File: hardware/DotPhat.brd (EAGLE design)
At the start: 30 x 65 mm, 39 parts, among them CN1 1X4-BIG, IC1 CAT24M010TS, J2 RASPBERRYPI-40-PIN-GPIO_PTH, J3 USB-MICROB, U1 ATMEGA328P-MU-QFN32, U2 TMP102, U3 ATSHA204-TSU, X3 S4B-ZR

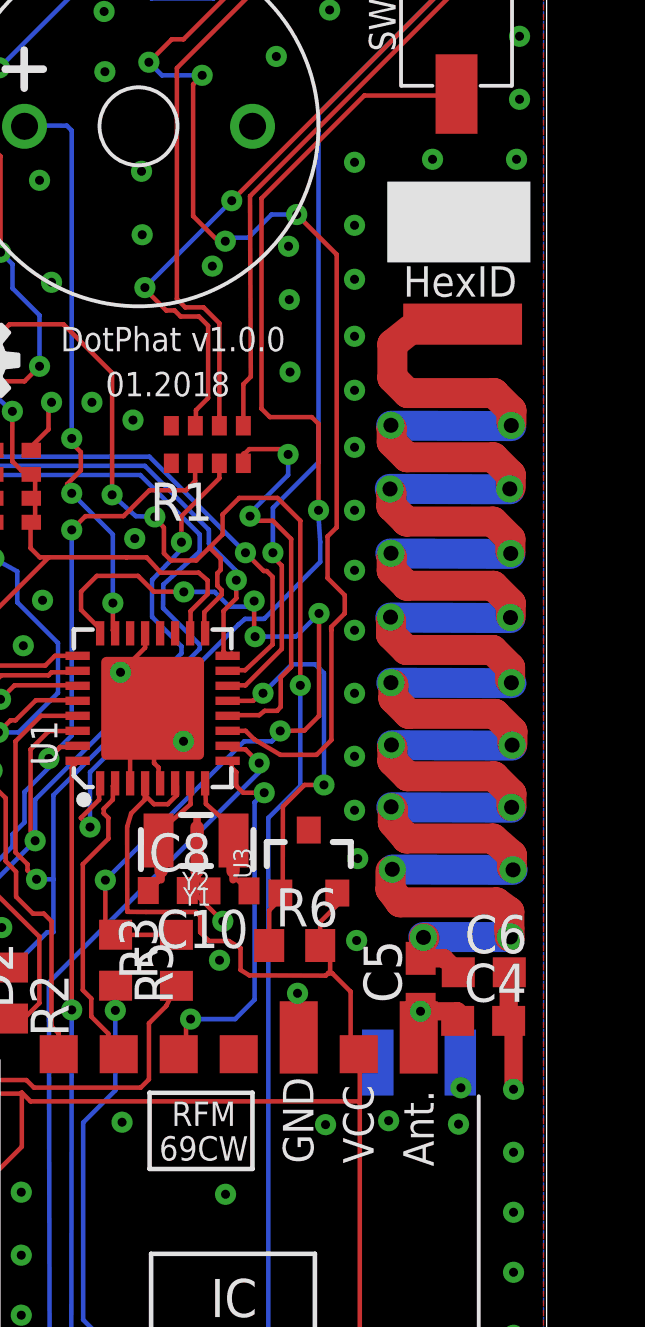
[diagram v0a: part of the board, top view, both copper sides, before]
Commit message: Flip uFL to top side
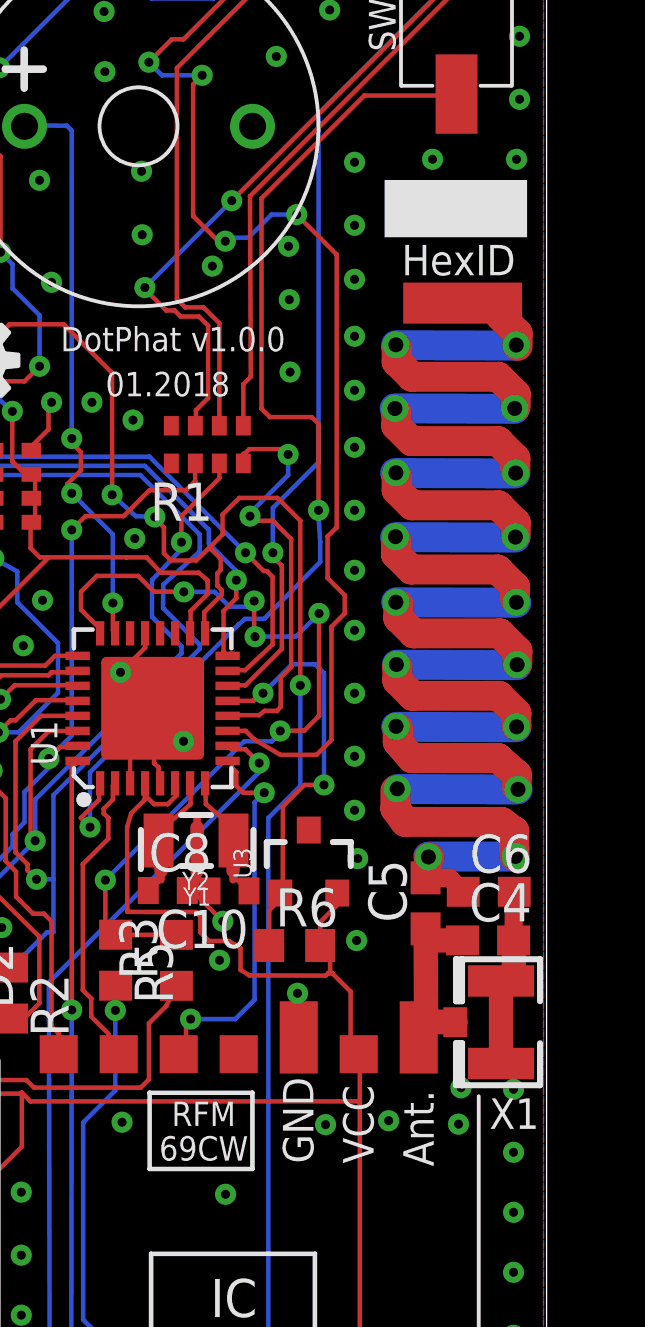
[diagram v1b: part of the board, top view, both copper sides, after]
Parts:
- moved X1 3.05 mm to (28.5, 21.5), flipped to the top, turned to 180 degrees
- moved C4 2.69 mm to (28.1, 24.3)
- moved C5 2.69 mm to (26.0, 25.5)
- moved C6 2.69 mm to (28.1, 25.9)
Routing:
- net ANT: track 86.7 -> 80.0 mm
- net ANT_OUT: track 3.57 -> 7.32 mm, vias 1 -> 0
- net GND: track 52.1 -> 54.0 mm
- net ANT2: track 0.00 -> 1.24 mm

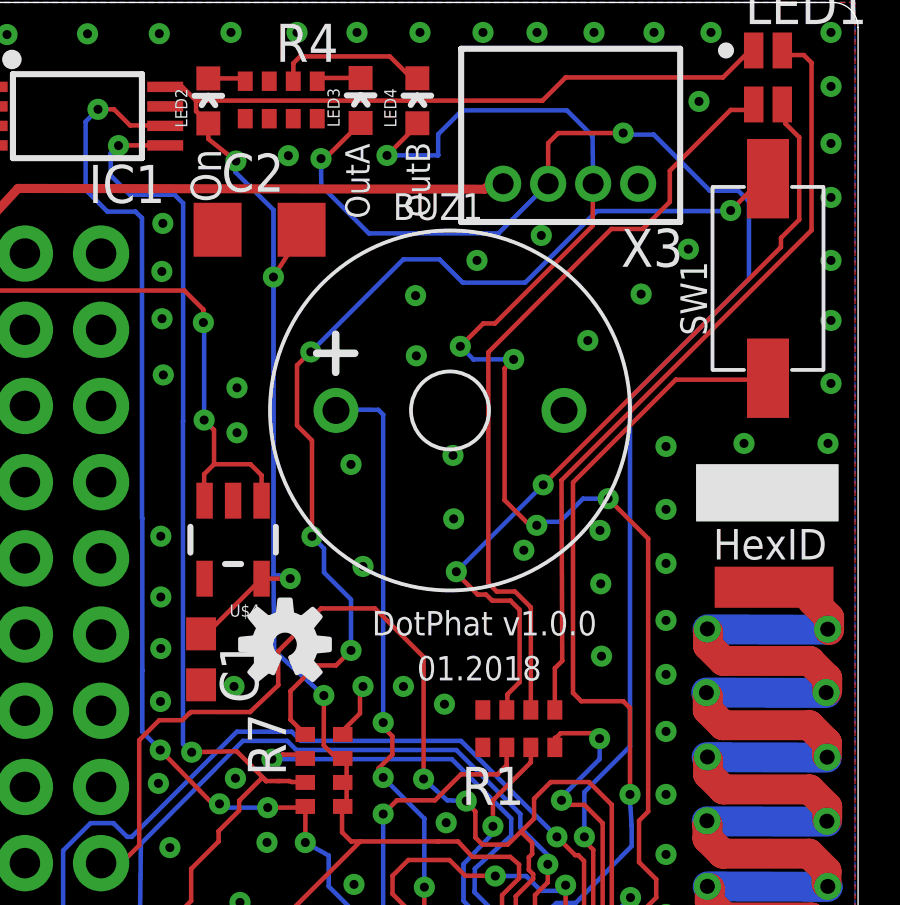
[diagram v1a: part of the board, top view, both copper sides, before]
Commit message: Switch to SMD buzzer
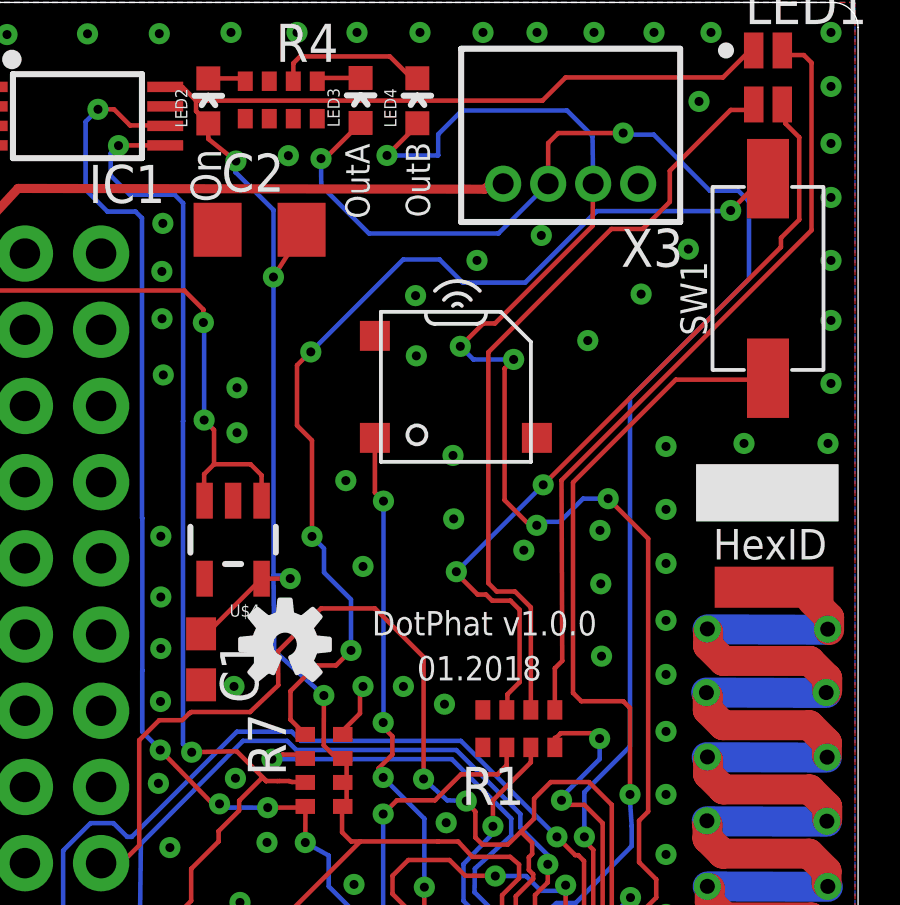
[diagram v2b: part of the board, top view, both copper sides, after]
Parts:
- removed BUZ1: KS-12065D03YA, Seeed-OPL-Connector:BZ2-7.6-D12.0XH6.5MM
- added SPK1: SMT-0540-S-R, adafruit:SMT-0540-S-R
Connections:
- net BUZZER: now also SPK1.+; no longer BUZ1.+
- net GND: now also SPK1.-; no longer BUZ1.-
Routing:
- net BUZZER: track 19.4 -> 17.1 mm, vias 3 -> 4
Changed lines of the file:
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@@
 <attribute name="PROD_ID" value="CONN-12263" x="3.5" y="32.5" size="1.778" layer="27" rot="R180" display="off"/>
-</element>
-<element name="BUZ1" library="Seeed-OPL-Connector" package="BZ2-7.6-D12.0XH6.5MM" value="KS-12065D03YA" x="16.4" y="51.4">
-<attribute name="MPN" value="KS-12065D03YA" x="16.4" y="51.4" size="1.778" layer="27" display="off"/>
 </element>
 <element name="LOGO1" library="Spark" package="OSHW-LOGO-S" value="OSHW-LOGOS" x="10.9" y="43.6"/>
@@
 <element name="C8" library="rcl" package="C0402" value="" x="17.37588125" y="25.925521875"/>
 <element name="C10" library="rcl" package="C0402" value="" x="19.432271875" y="25.914353125" rot="R180"/>
+<element name="SPK1" library="adafruit" package="SMT-0540-S-R" value="SMT-0540-S-R" x="16.596359375" y="52.18633125" rot="R270"/>
 </elements>
 <signals>
@@
 <contactref element="X1" pad="2"/>
 <contactref element="Y1" pad="2"/>
-<contactref element="BUZ1" pad="-"/>
 <contactref element="R7" pad="8"/>
 <contactref element="J2" pad="6"/>
@@
 <via x="17.3" y="56.4" extent="1-16" drill="0.3"/>
 <via x="9.3" y="52.1556" extent="1-16" drill="0.3"/>
-<via x="13.1" y="49.6" extent="1-16" drill="0.3"/>
+<via x="12.926771875" y="49.06075625" extent="1-16" drill="0.3"/>
 <via x="16.5" y="49.9" extent="1-16" drill="0.3"/>
 <via x="11.520140625" y="29.9230625" extent="1-16" drill="0.3"/>
@@
 <wire x1="28.89720625" y1="22.9469875" x2="28.484275" y2="22.910665625" width="0.8128" layer="1"/>
 <wire x1="28.484275" y1="20.160665625" x2="28.484275" y2="22.910665625" width="0.8128" layer="1"/>
+<contactref element="SPK1" pad="-"/>
 </signal>
 <signal name="SDA">
@@
 <signal name="BUZZER">
 <contactref element="U1" pad="23"/>
-<contactref element="BUZ1" pad="+"/>
 <wire x1="15.5448" y1="35.5092" x2="15.5448" y2="34.5948" width="0.1524" layer="1"/>
 <wire x1="15.5448" y1="37.7952" x2="15.5448" y2="35.5092" width="0.1524" layer="16"/>
@@
 <wire x1="14.1732" y1="40.8432" x2="14.478" y2="40.5384" width="0.1524" layer="1"/>
 <wire x1="14.1732" y1="40.9956" x2="14.1732" y2="40.8432" width="0.1524" layer="1"/>
-<wire x1="14.1732" y1="51.2588" x2="14.1732" y2="40.9956" width="0.1524" layer="16"/>
-<wire x1="14.0112" y1="51.4208" x2="14.1732" y2="51.2588" width="0.1524" layer="16"/>
-<wire x1="12.6112" y1="51.4304" x2="14.0112" y2="51.4208" width="0.1524" layer="16"/>
 <wire x1="15.5448" y1="34.5948" x2="15.62" y2="34.5" width="0.1524" layer="1"/>
-<wire x1="12.6112" y1="51.4304" x2="12.6" y2="51.4" width="0.1524" layer="16"/>
 <via x="15.5448" y="35.5092" extent="1-16" drill="0.3"/>
 <via x="14.1732" y="39.1668" extent="1-16" drill="0.3"/>
 <via x="14.1732" y="40.9956" extent="1-16" drill="0.3"/>
+<contactref element="SPK1" pad="+"/>
+<wire x1="14.1732" y1="40.9956" x2="14.18234375" y2="40.9956" width="0.1524" layer="16"/>
+<wire x1="14.18234375" y1="40.9956" x2="14.18234375" y2="48.378109375" width="0.1524" layer="16"/>
+<via x="14.18234375" y="48.378109375" extent="1-16" drill="0.3"/>
+<wire x1="14.18234375" y1="48.378109375" x2="13.896359375" y2="48.66409375" width="0.1524" layer="1"/>
+<wire x1="13.896359375" y1="48.66409375" x2="13.896359375" y2="50.48633125" width="0.1524" layer="1"/>
 </signal>
 <signal name="OUTA">

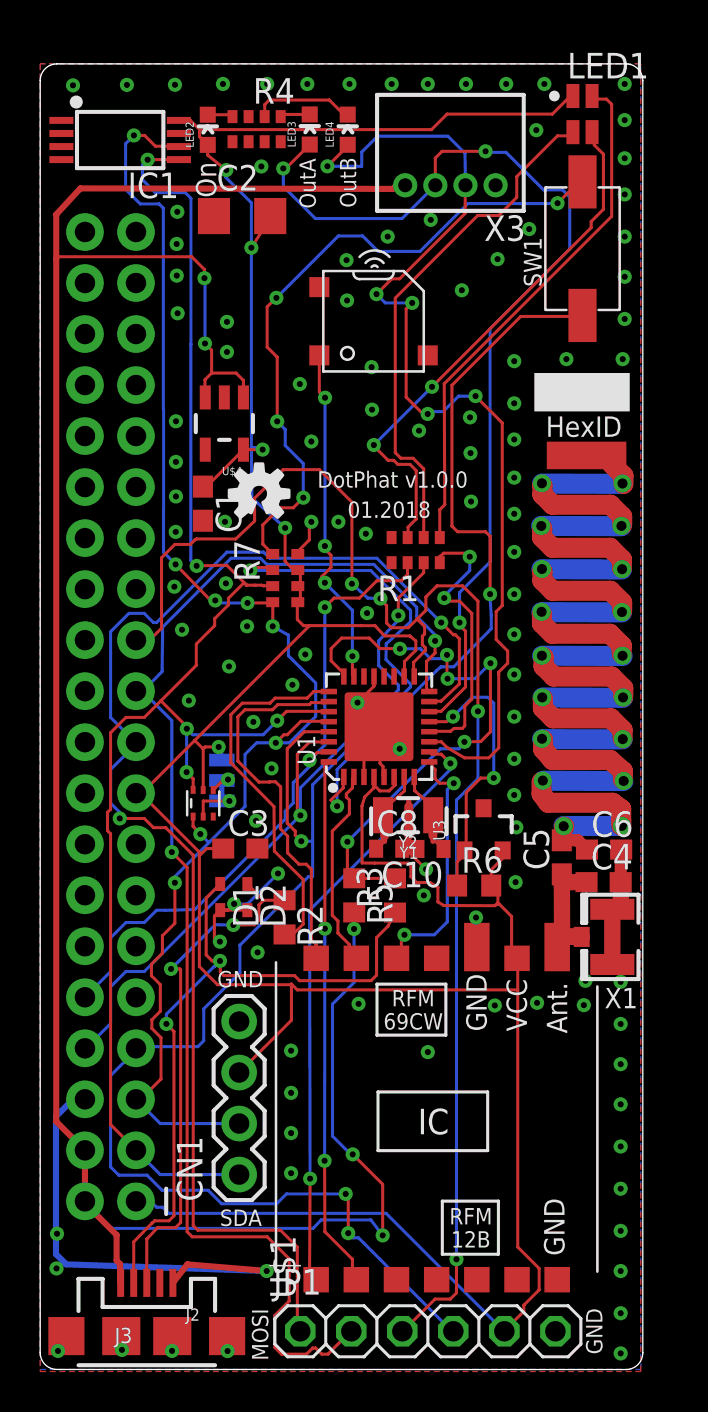
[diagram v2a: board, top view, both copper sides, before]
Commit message: Reposition antenna PI-filter
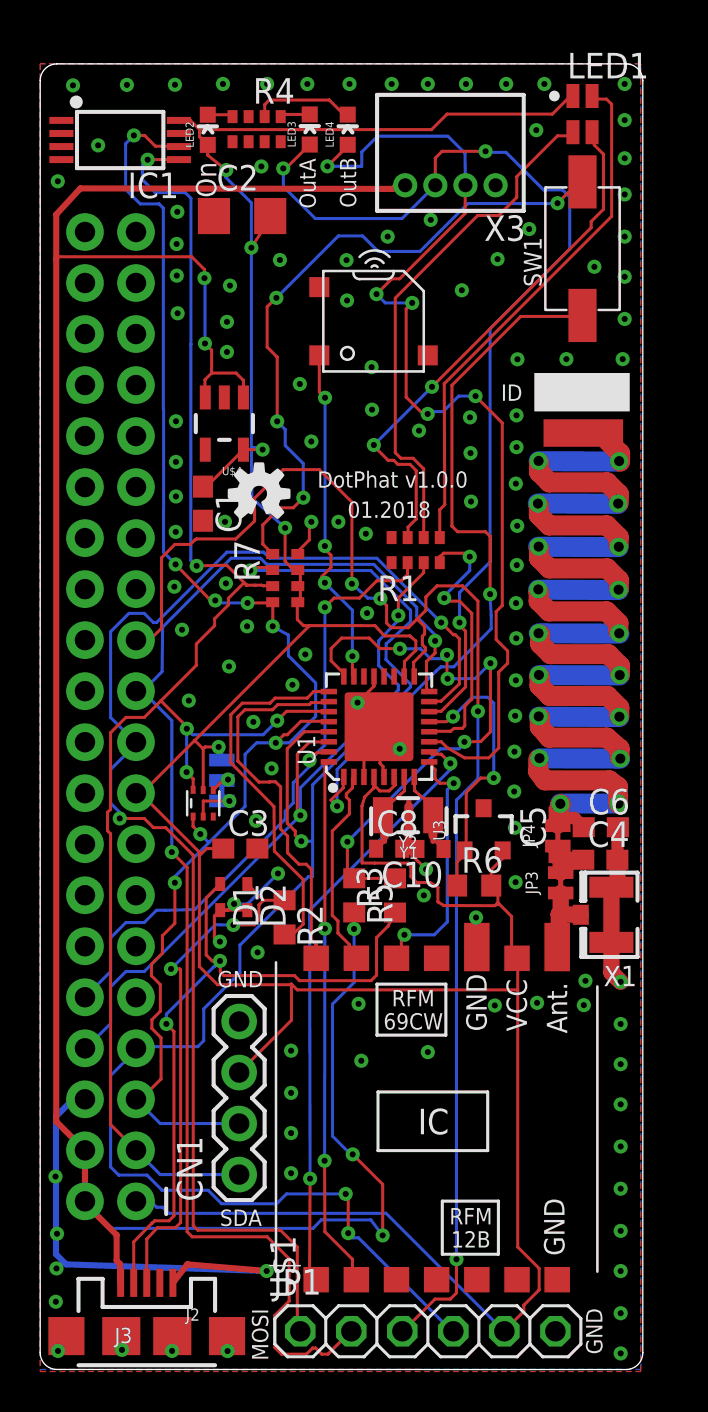
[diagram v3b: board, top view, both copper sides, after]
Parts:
- added JP3, JP4: JUMPER-SMT_2_NC_TRACE_NO-SILK, SparkFun-Jumpers:SMT-JUMPER_2_NC_TRACE_NO-SILK
- moved C4 1.13 mm to (27.9, 25.4)
- moved C5 1.13 mm to (25.8, 26.6)
- moved C6 1.13 mm to (27.9, 27.0)
- moved X1 1.10 mm to (28.4, 22.6)
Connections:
- new net N$3: C4.1, C5.1, JP3.2, JP4.1
- net ANT: now also JP4.2
- net ANT_OUT: now also JP3.1; no longer C4.1, C5.1
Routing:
- net ANT_OUT: track 7.32 -> 3.86 mm
- net N$3: track 0.00 -> 2.23 mm
- net GND: track 54.0 -> 56.0 mm, vias 115 -> 123
- net ANT: track 80.0 -> 81.1 mm
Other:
- board text added: "ID"
- board text removed: "HexID"

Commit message: Improve GND
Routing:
- net GND: vias 123 -> 127
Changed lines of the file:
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@@
 <setting verticaltext="up"/>
 </settings>
-<grid distance="0.1" unitdist="mm" unit="mm" style="lines" multiple="1" display="yes" altdistance="0.025" altunitdist="inch" altunit="inch"/>
+<grid distance="0.05" unitdist="mm" unit="mm" style="lines" multiple="1" display="yes" altdistance="0.025" altunitdist="inch" altunit="inch"/>
 <layers>
 <layer number="1" name="Top" color="4" fill="1" visible="yes" active="yes"/>
@@
 <via x="15.851334375" y="18.202840625" extent="1-16" drill="0.3"/>
 <via x="21.4" y="47.4" extent="1-16" drill="0.3"/>
-<via x="9.1" y="64" extent="1-16" drill="0.3"/>
-<via x="11.3" y="64" extent="1-16" drill="0.3"/>
-<via x="13.3" y="64" extent="1-16" drill="0.3"/>
-<via x="15.4" y="64" extent="1-16" drill="0.3"/>
-<via x="17.5" y="64" extent="1-16" drill="0.3"/>
-<via x="19.3" y="64" extent="1-16" drill="0.3"/>
-<via x="21.2" y="64" extent="1-16" drill="0.3"/>
+<via x="10.6" y="64" extent="1-16" drill="0.3"/>
+<via x="12.5" y="64" extent="1-16" drill="0.3"/>
+<via x="14.3" y="64" extent="1-16" drill="0.3"/>
+<via x="16.1" y="64" extent="1-16" drill="0.3"/>
+<via x="17.9" y="64" extent="1-16" drill="0.3"/>
+<via x="19.7" y="64" extent="1-16" drill="0.3"/>
+<via x="21.5" y="64" extent="1-16" drill="0.3"/>
 <via x="23.2" y="64" extent="1-16" drill="0.3"/>
 <via x="25.1" y="64" extent="1-16" drill="0.3"/>
 <via x="24.7" y="61.7" extent="1-16" drill="0.3"/>
-<via x="1.63365625" y="63.929865625" extent="1-16" drill="0.3"/>
+<via x="5.13365625" y="63.929865625" extent="1-16" drill="0.3"/>
 <via x="17.3" y="56.4" extent="1-16" drill="0.3"/>
 <via x="9.3" y="52.1556" extent="1-16" drill="0.3"/>
@@
 <via x="15.2526" y="55.2276" extent="1-16" drill="0.3"/>
 <via x="19.4436" y="57.2342" extent="1-16" drill="0.3"/>
-<via x="6.709565625" y="63.959865625" extent="1-16" drill="0.3"/>
-<via x="4.317390625" y="63.954025" extent="1-16" drill="0.3"/>
+<via x="8.709565625" y="64.009865625" extent="1-16" drill="0.3"/>
+<via x="6.917390625" y="63.954025" extent="1-16" drill="0.3"/>
 <via x="6.679846875" y="38.969821875" extent="1-16" drill="0.3"/>
 <via x="6.748621875" y="41.69844375" extent="1-16" drill="0.3"/>
@@
 <via x="0.87694375" y="59.152853125" extent="1-16" drill="0.3"/>
 <via x="2.885828125" y="60.94380625" extent="1-16" drill="0.3"/>
+<via x="3.13365625" y="63.929865625" extent="1-16" drill="0.3"/>
+<via x="1.13365625" y="63.929865625" extent="1-16" drill="0.3"/>
+<via x="6.386209375" y="6.071765625" extent="1-16" drill="0.3"/>
+<via x="9.386209375" y="3.971765625" extent="1-16" drill="0.3"/>
 </signal>
 <signal name="SDA">

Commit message: checkpoint
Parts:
- moved C2 1.12 mm to (10.5, 56.4)
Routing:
- net +3V3: track 174.2 -> 174.9 mm
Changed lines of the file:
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@@
 <setting verticaltext="up"/>
 </settings>
-<grid distance="0.05" unitdist="mm" unit="mm" style="lines" multiple="1" display="yes" altdistance="0.025" altunitdist="inch" altunit="inch"/>
+<grid distance="0.005" unitdist="mm" unit="mm" style="lines" multiple="1" display="yes" altdistance="0.025" altunitdist="inch" altunit="inch"/>
 <layers>
 <layer number="1" name="Top" color="4" fill="1" visible="yes" active="yes"/>
@@
 <rectangle x1="23.6474" y1="7.6454" x2="24.8158" y2="7.6708" layer="22" rot="R270"/>
 <text x="26.6446" y="13.5636" size="1.27" layer="22" rot="SMR0">Mihai Galos</text>
-<text x="8.770875" y="58.335671875" size="1.016" layer="21" rot="R90">On</text>
+<text x="8.730875" y="58.235671875" size="1.016" layer="21" rot="R90">On</text>
 <rectangle x1="25.05735625" y1="45.9359" x2="29.01975625" y2="47.3075" layer="1"/>
-<rectangle x1="25.2222" y1="44.82109375" x2="29.1846" y2="46.19269375" layer="29"/>
+<rectangle x1="25.0472" y1="45.94109375" x2="29.0096" y2="47.31269375" layer="29"/>
 <text x="11.04239375" y="7.958075" size="0.8128" layer="21" rot="R180">SDA</text>
 <text x="11.116053125" y="19.838415625" size="0.8128" layer="21" rot="R180">GND</text>
@@
 </element>
 <element name="R6" library="rcl" package="R0603" value="" x="21.606" y="24.0926625"/>
-<element name="C2" library="rcl" package="C3216" value="" x="10.052809375" y="57.422284375"/>
+<element name="C2" library="rcl" package="C3216" value="" x="10.467809375" y="56.387284375"/>
 <element name="C4" library="rcl" package="C0603" value="" x="27.88691875" y="25.3779"/>
 <element name="C5" library="rcl" package="C0603" value="" x="25.805384375" y="26.61285" rot="R90"/>
@@
 <wire x1="10.54074375" y1="43.3903125" x2="10.5156" y2="45.8978" width="0.1524" layer="16"/>
 <wire x1="10.5156" y1="45.8978" x2="10.5156" y2="55.860440625" width="0.1524" layer="16"/>
-<wire x1="10.5156" y1="55.860440625" x2="10.5156" y2="58.0844" width="0.1524" layer="16"/>
+<wire x1="10.5156" y1="55.860440625" x2="10.5156" y2="57.825" width="0.1524" layer="16"/>
+<wire x1="10.5156" y1="57.825" x2="10.5156" y2="58.0844" width="0.1524" layer="16"/>
 <wire x1="10.5156" y1="58.0844" x2="9.247621875" y2="59.3412" width="0.1524" layer="16"/>
 <contactref element="CN1" pad="3"/>
@@
 <wire x1="22.456" y1="24.0926625" x2="22.456" y2="24.87560625" width="0.1524" layer="1"/>
 <contactref element="C2" pad="2"/>
-<wire x1="11.452809375" y1="57.422284375" x2="11.452809375" y2="57.31631875" width="0.1524" layer="1"/>
-<wire x1="11.452809375" y1="57.31631875" x2="10.513821875" y2="55.846471875" width="0.1524" layer="1"/>
-<via x="10.513821875" y="55.846471875" extent="1-16" drill="0.3"/>
 <wire x1="10.513821875" y1="55.846471875" x2="10.50721875" y2="55.852059375" width="0.1524" layer="16"/>
 <wire x1="10.50721875" y1="55.852059375" x2="10.5156" y2="55.860440625" width="0.1524" layer="16"/>
@@
 <wire x1="16.6075375" y1="28.951428125" x2="16.6075375" y2="29.4875375" width="0.1524" layer="1"/>
 <wire x1="16.6075375" y1="29.4875375" x2="16.62" y2="29.5" width="0.1524" layer="1"/>
+<wire x1="11.867809375" y1="56.387284375" x2="11.867809375" y2="57.422190625" width="0.1524" layer="1"/>
+<wire x1="11.867809375" y1="57.422190625" x2="11.505" y2="57.785" width="0.1524" layer="1"/>
+<via x="11.505" y="57.785" extent="1-16" drill="0.3"/>
+<wire x1="11.505" y1="57.785" x2="10.5556" y2="57.785" width="0.1524" layer="16"/>
+<wire x1="10.5556" y1="57.785" x2="10.5156" y2="57.825" width="0.1524" layer="16"/>
 </signal>
 <signal name="ADCENA">

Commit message: Improve GND
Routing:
- net GND: vias 127 -> 129
